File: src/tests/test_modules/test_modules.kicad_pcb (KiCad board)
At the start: 2 copper layers, 29.2 x 16.5 mm, 3 parts, among them U1 LM555, U2 LM555, U3 8255

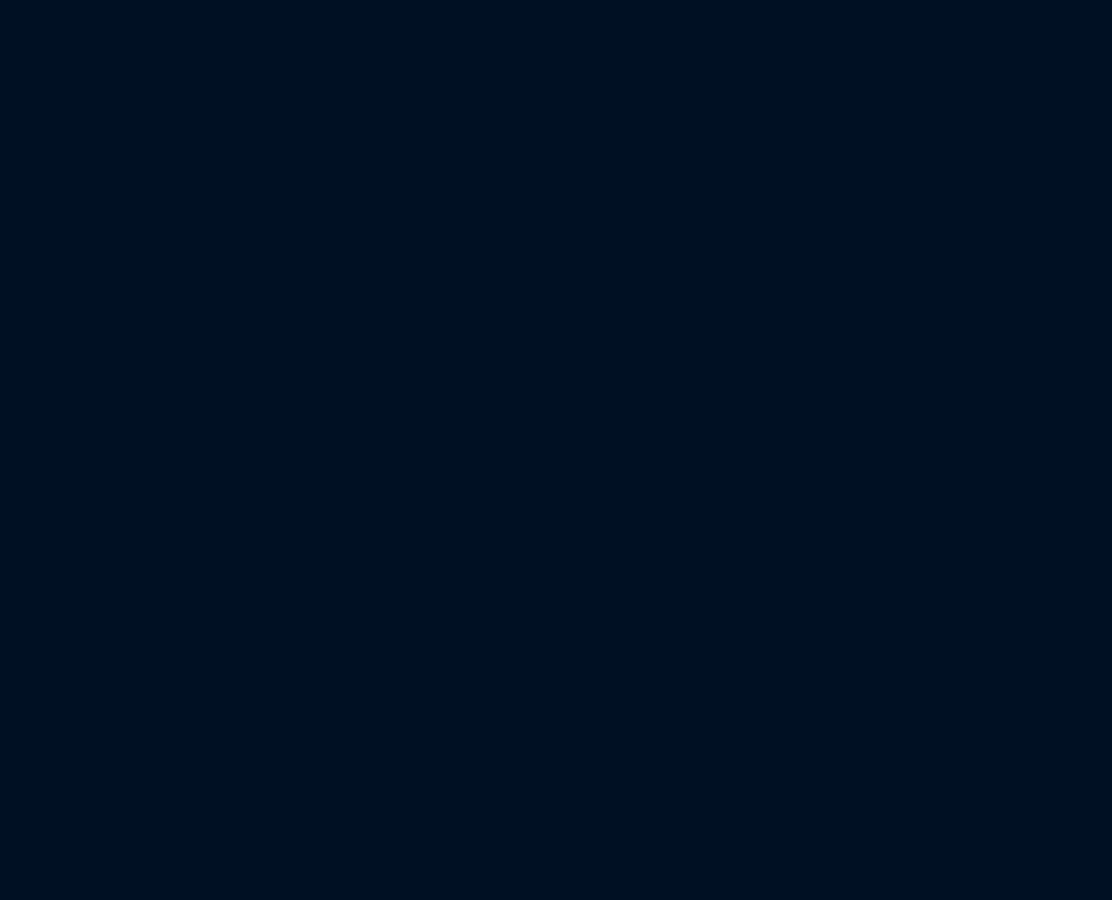
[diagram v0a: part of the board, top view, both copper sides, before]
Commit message: Add new keywords (#11)
Added new keywords:
`Modules Should Have Values Matching` - validate that selected modules have valid values.
`Complement Modules By Reference` - perform set complement operation on module lists.
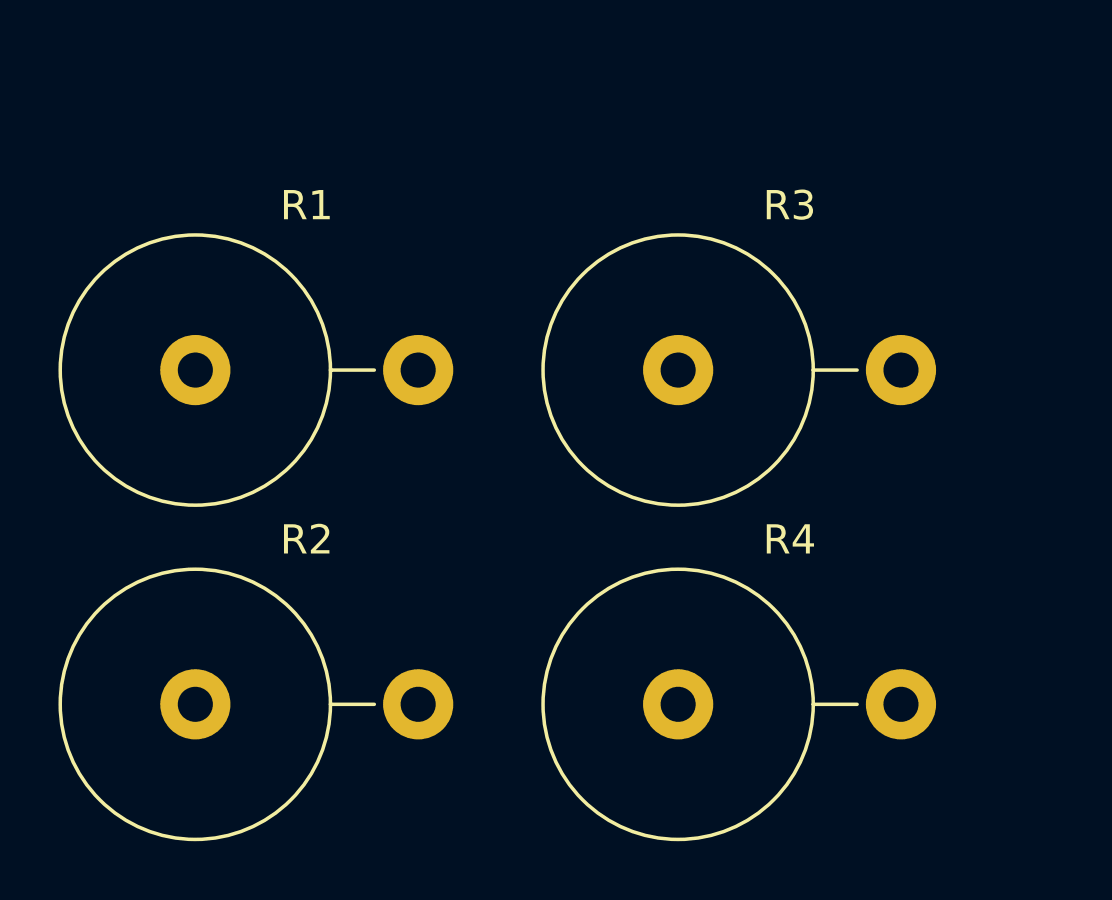
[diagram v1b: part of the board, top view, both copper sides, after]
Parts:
- added R1: 10k, Resistor_THT:R_Axial_DIN0922_L20.0mm_D9.0mm_P7.62mm_Vertical, F.Cu at (71.1, 74.9)
- added R2: 330, Resistor_THT:R_Axial_DIN0922_L20.0mm_D9.0mm_P7.62mm_Vertical, F.Cu at (71.1, 86.4)
- added R3: 2 M, Resistor_THT:R_Axial_DIN0922_L20.0mm_D9.0mm_P7.62mm_Vertical, F.Cu at (87.6, 74.9)
- added R4: 0.1uF, Resistor_THT:R_Axial_DIN0922_L20.0mm_D9.0mm_P7.62mm_Vertical, F.Cu at (87.6, 86.4)
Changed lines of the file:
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@@
     (tracks 39)
     (zones 0)
-    (modules 3)
-    (nets 49)
+    (modules 7)
+    (nets 57)
   )
   (page A4)
@@
   (net 47 "Net-(U3-Pad20)")
   (net 48 "Net-(U3-Pad40)")
+  (net 49 "Net-(R1-Pad1)")
+  (net 50 "Net-(R1-Pad2)")
+  (net 51 "Net-(R2-Pad2)")
+  (net 52 "Net-(R2-Pad1)")
+  (net 53 "Net-(R3-Pad1)")
+  (net 54 "Net-(R3-Pad2)")
+  (net 55 "Net-(R4-Pad2)")
+  (net 56 "Net-(R4-Pad1)")
   (net_class Default "This is the default net class."
     (clearance 0.2)
@@
     (add_net /~R)
     (add_net GND)
+    (add_net "Net-(R1-Pad1)")
+    (add_net "Net-(R1-Pad2)")
+    (add_net "Net-(R2-Pad1)")
+    (add_net "Net-(R2-Pad2)")
+    (add_net "Net-(R3-Pad1)")
+    (add_net "Net-(R3-Pad2)")
+    (add_net "Net-(R4-Pad1)")
+    (add_net "Net-(R4-Pad2)")
     (add_net "Net-(U3-Pad1)")
     (add_net "Net-(U3-Pad10)")
@@
     (add_net VCC)
   )
+  (module Resistor_THT:R_Axial_DIN0922_L20.0mm_D9.0mm_P7.62mm_Vertical (layer F.Cu)
+    (at 87.63 86.36)
+    (descr "Resistor, Axial_DIN0922 series, Axial, Vertical, pin pitch=7.62mm, 5W, length*diameter=20*9mm^2, http://www.vishay.com/docs/20128/wkxwrx.pdf")
+    (tags "Resistor Axial_DIN0922 series Axial Vertical pin pitch 7.62mm 5W length 20mm diameter 9mm")
+    (fp_text reference R4 (at 3.81 -5.62) (layer F.SilkS)
+      (effects (font (size 1 1) (thickness 0.15)))
+    )
+    (fp_text value 0.1uF (at 3.81 5.62) (layer F.Fab)
+      (effects (font (size 1 1) (thickness 0.15)))
+    )
+    (fp_text user %R (at 0 -1.7) (layer F.Fab)
+      (effects (font (size 1 1) (thickness 0.15)))
+    )
+    (fp_line (start 9.07 -4.75) (end -4.75 -4.75) (layer F.CrtYd) (width 0.05))
+    (fp_line (start 9.07 4.75) (end 9.07 -4.75) (layer F.CrtYd) (width 0.05))
+    (fp_line (start -4.75 4.75) (end 9.07 4.75) (layer F.CrtYd) (width 0.05))
+    (fp_line (start -4.75 -4.75) (end -4.75 4.75) (layer F.CrtYd) (width 0.05))
+    (fp_line (start 4.62 0) (end 6.12 0) (layer F.SilkS) (width 0.12))
+    (fp_line (start 0 0) (end 7.62 0) (layer F.Fab) (width 0.1))
+    (fp_circle (center 0 0) (end 4.62 0) (layer F.SilkS) (width 0.12))
+    (fp_circle (center 0 0) (end 4.5 0) (layer F.Fab) (width 0.1))
+    (pad 2 thru_hole oval (at 7.62 0) (size 2.4 2.4) (drill 1.2) (layers *.Cu *.Mask)
+      (net 55 "Net-(R4-Pad2)"))
+    (pad 1 thru_hole circle (at 0 0) (size 2.4 2.4) (drill 1.2) (layers *.Cu *.Mask)
+      (net 56 "Net-(R4-Pad1)"))
+    (model ${KISYS3DMOD}/Resistor_THT.3dshapes/R_Axial_DIN0922_L20.0mm_D9.0mm_P7.62mm_Vertical.wrl
+      (at (xyz 0 0 0))
+      (scale (xyz 1 1 1))
+      (rotate (xyz 0 0 0))
+    )
+  )
+  (module Resistor_THT:R_Axial_DIN0922_L20.0mm_D9.0mm_P7.62mm_Vertical (layer F.Cu)
+    (at 87.63 74.93)
+    (descr "Resistor, Axial_DIN0922 series, Axial, Vertical, pin pitch=7.62mm, 5W, length*diameter=20*9mm^2, http://www.vishay.com/docs/20128/wkxwrx.pdf")
+    (tags "Resistor Axial_DIN0922 series Axial Vertical pin pitch 7.62mm 5W length 20mm diameter 9mm")
+    (fp_text reference R3 (at 3.81 -5.62) (layer F.SilkS)
+      (effects (font (size 1 1) (thickness 0.15)))
+    )
+    (fp_text value "2 M" (at 3.81 5.62) (layer F.Fab)
+      (effects (font (size 1 1) (thickness 0.15)))
+    )
+    (fp_circle (center 0 0) (end 4.5 0) (layer F.Fab) (width 0.1))
+    (fp_circle (center 0 0) (end 4.62 0) (layer F.SilkS) (width 0.12))
+    (fp_line (start 0 0) (end 7.62 0) (layer F.Fab) (width 0.1))
+    (fp_line (start 4.62 0) (end 6.12 0) (layer F.SilkS) (width 0.12))
+    (fp_line (start -4.75 -4.75) (end -4.75 4.75) (layer F.CrtYd) (width 0.05))
+    (fp_line (start -4.75 4.75) (end 9.07 4.75) (layer F.CrtYd) (width 0.05))
+    (fp_line (start 9.07 4.75) (end 9.07 -4.75) (layer F.CrtYd) (width 0.05))
+    (fp_line (start 9.07 -4.75) (end -4.75 -4.75) (layer F.CrtYd) (width 0.05))
+    (fp_text user %R (at 0 -1.7) (layer F.Fab)
+      (effects (font (size 1 1) (thickness 0.15)))
+    )
+    (pad 1 thru_hole circle (at 0 0) (size 2.4 2.4) (drill 1.2) (layers *.Cu *.Mask)
+      (net 53 "Net-(R3-Pad1)"))
+    (pad 2 thru_hole oval (at 7.62 0) (size 2.4 2.4) (drill 1.2) (layers *.Cu *.Mask)
+      (net 54 "Net-(R3-Pad2)"))
+    (model ${KISYS3DMOD}/Resistor_THT.3dshapes/R_Axial_DIN0922_L20.0mm_D9.0mm_P7.62mm_Vertical.wrl
+      (at (xyz 0 0 0))
+      (scale (xyz 1 1 1))
+      (rotate (xyz 0 0 0))
+    )
+  )
+  (module Resistor_THT:R_Axial_DIN0922_L20.0mm_D9.0mm_P7.62mm_Vertical (layer F.Cu)
+    (at 71.12 86.36)
+    (descr "Resistor, Axial_DIN0922 series, Axial, Vertical, pin pitch=7.62mm, 5W, length*diameter=20*9mm^2, http://www.vishay.com/docs/20128/wkxwrx.pdf")
+    (tags "Resistor Axial_DIN0922 series Axial Vertical pin pitch 7.62mm 5W length 20mm diameter 9mm")
+    (fp_text reference R2 (at 3.81 -5.62) (layer F.SilkS)
+      (effects (font (size 1 1) (thickness 0.15)))
+    )
+    (fp_text value 330 (at 3.81 5.62) (layer F.Fab)
+      (effects (font (size 1 1) (thickness 0.15)))
+    )
+    (fp_text user %R (at 0 -1.7) (layer F.Fab)
+      (effects (font (size 1 1) (thickness 0.15)))
+    )
+    (fp_line (start 9.07 -4.75) (end -4.75 -4.75) (layer F.CrtYd) (width 0.05))
+    (fp_line (start 9.07 4.75) (end 9.07 -4.75) (layer F.CrtYd) (width 0.05))
+    (fp_line (start -4.75 4.75) (end 9.07 4.75) (layer F.CrtYd) (width 0.05))
+    (fp_line (start -4.75 -4.75) (end -4.75 4.75) (layer F.CrtYd) (width 0.05))
+    (fp_line (start 4.62 0) (end 6.12 0) (layer F.SilkS) (width 0.12))
+    (fp_line (start 0 0) (end 7.62 0) (layer F.Fab) (width 0.1))
+    (fp_circle (center 0 0) (end 4.62 0) (layer F.SilkS) (width 0.12))
+    (fp_circle (center 0 0) (end 4.5 0) (layer F.Fab) (width 0.1))
+    (pad 2 thru_hole oval (at 7.62 0) (size 2.4 2.4) (drill 1.2) (layers *.Cu *.Mask)
+      (net 51 "Net-(R2-Pad2)"))
+    (pad 1 thru_hole circle (at 0 0) (size 2.4 2.4) (drill 1.2) (layers *.Cu *.Mask)
+      (net 52 "Net-(R2-Pad1)"))
+    (model ${KISYS3DMOD}/Resistor_THT.3dshapes/R_Axial_DIN0922_L20.0mm_D9.0mm_P7.62mm_Vertical.wrl
+      (at (xyz 0 0 0))
+      (scale (xyz 1 1 1))
+      (rotate (xyz 0 0 0))
+    )
+  )
+  (module Resistor_THT:R_Axial_DIN0922_L20.0mm_D9.0mm_P7.62mm_Vertical (layer F.Cu)
+    (at 71.12 74.93)
+    (descr "Resistor, Axial_DIN0922 series, Axial, Vertical, pin pitch=7.62mm, 5W, length*diameter=20*9mm^2, http://www.vishay.com/docs/20128/wkxwrx.pdf")
+    (tags "Resistor Axial_DIN0922 series Axial Vertical pin pitch 7.62mm 5W length 20mm diameter 9mm")
+    (fp_text reference R1 (at 3.81 -5.62) (layer F.SilkS)
+      (effects (font (size 1 1) (thickness 0.15)))
+    )
+    (fp_text value 10k (at 3.81 5.62) (layer F.Fab)
+      (effects (font (size 1 1) (thickness 0.15)))
+    )
+    (fp_circle (center 0 0) (end 4.5 0) (layer F.Fab) (width 0.1))
+    (fp_circle (center 0 0) (end 4.62 0) (layer F.SilkS) (width 0.12))
+    (fp_line (start 0 0) (end 7.62 0) (layer F.Fab) (width 0.1))
+    (fp_line (start 4.62 0) (end 6.12 0) (layer F.SilkS) (width 0.12))
+    (fp_line (start -4.75 -4.75) (end -4.75 4.75) (layer F.CrtYd) (width 0.05))
+    (fp_line (start -4.75 4.75) (end 9.07 4.75) (layer F.CrtYd) (width 0.05))
+    (fp_line (start 9.07 4.75) (end 9.07 -4.75) (layer F.CrtYd) (width 0.05))
+    (fp_line (start 9.07 -4.75) (end -4.75 -4.75) (layer F.CrtYd) (width 0.05))
+    (fp_text user %R (at 0 -1.7) (layer F.Fab)
+      (effects (font (size 1 1) (thickness 0.15)))
+    )
+    (pad 1 thru_hole circle (at 0 0) (size 2.4 2.4) (drill 1.2) (layers *.Cu *.Mask)
+      (net 49 "Net-(R1-Pad1)"))
+    (pad 2 thru_hole oval (at 7.62 0) (size 2.4 2.4) (drill 1.2) (layers *.Cu *.Mask)
+      (net 50 "Net-(R1-Pad2)"))
+    (model ${KISYS3DMOD}/Resistor_THT.3dshapes/R_Axial_DIN0922_L20.0mm_D9.0mm_P7.62mm_Vertical.wrl
+      (at (xyz 0 0 0))
+      (scale (xyz 1 1 1))
+      (rotate (xyz 0 0 0))
+    )
+  )
   (module Package_DIP:DIP-40_W15.24mm (layer F.Cu)

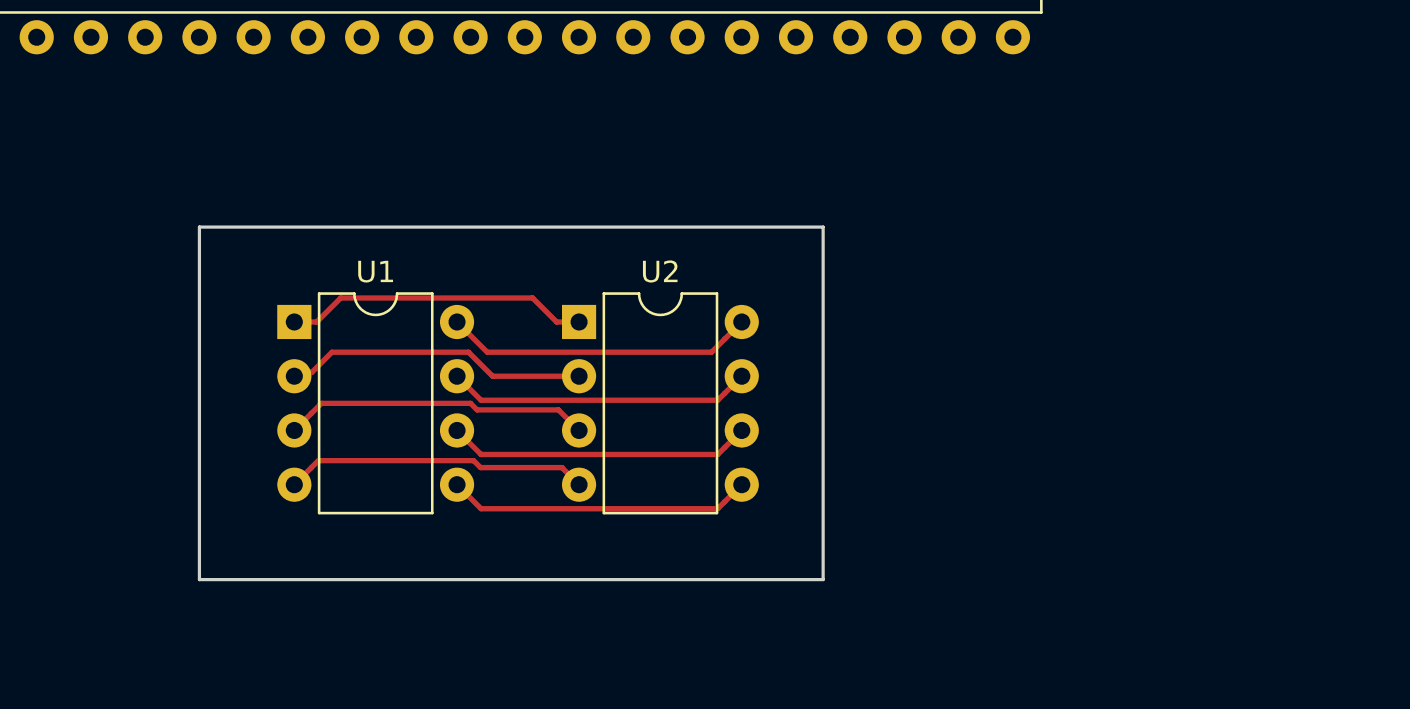
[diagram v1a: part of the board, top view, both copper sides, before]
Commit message: Adapt to newer versions of Robot Framework and KiCad, updating FOR loop syntax as well as deprecating LM555. Ensure Python3 is used. Stop building for Python 2.7 Fix code smell (is not -> !=). Update security token for GH releases.
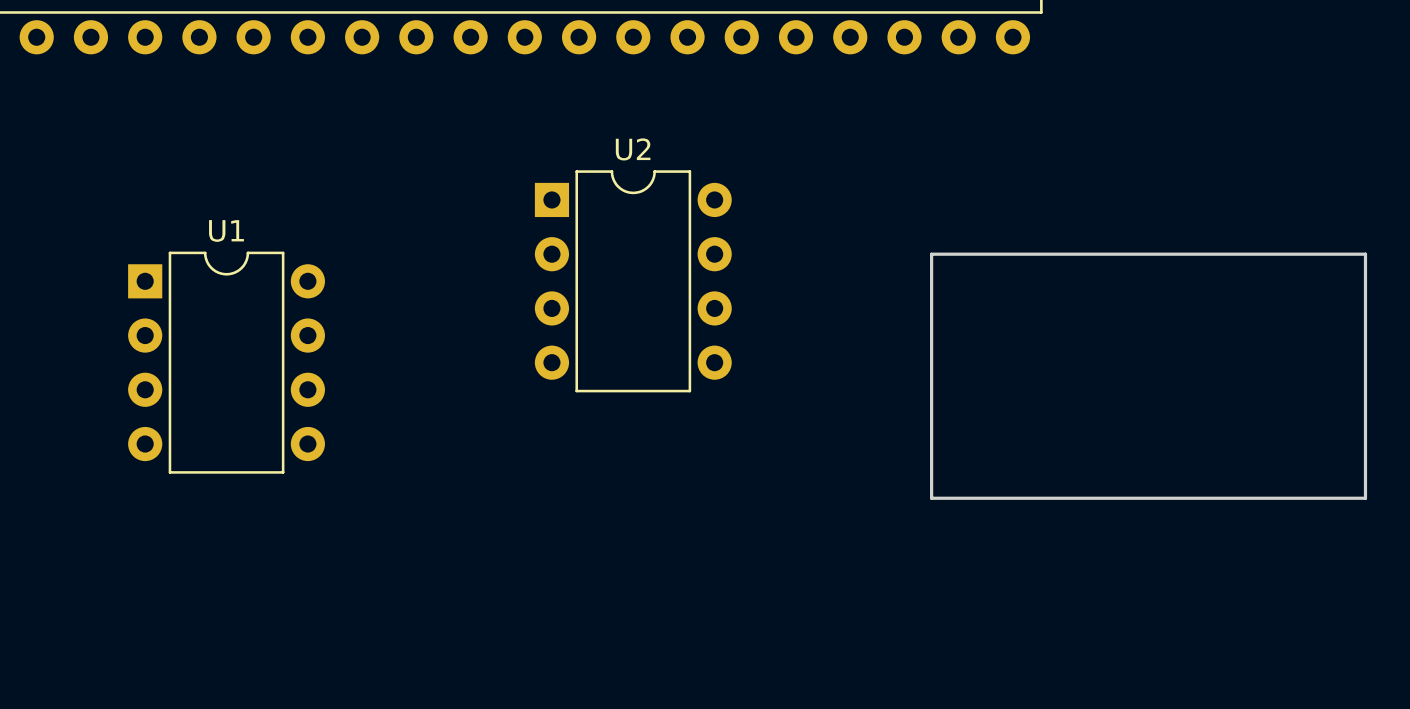
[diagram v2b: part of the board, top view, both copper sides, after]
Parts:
- U1, U2: value LM555 -> NA555P
- moved U1 7.24 mm to (116.8, 71.1)
- moved U2 5.85 mm to (135.9, 67.3)
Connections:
- R1 pad 1: Net-(R1-Pad1) -> (no net)
- R1 pad 2: Net-(R1-Pad2) -> (no net)
- R2 pad 1: Net-(R2-Pad1) -> (no net)
- R2 pad 2: Net-(R2-Pad2) -> (no net)
- R3 pad 1: Net-(R3-Pad1) -> (no net)
- R3 pad 2: Net-(R3-Pad2) -> (no net)
- R4 pad 1: Net-(R4-Pad1) -> (no net)
- R4 pad 2: Net-(R4-Pad2) -> (no net)
- U3 pad 1: Net-(U3-Pad1) -> (no net)
- U3 pad 10: Net-(U3-Pad10) -> (no net)
- U3 pad 11: Net-(U3-Pad11) -> (no net)
- U3 pad 12: Net-(U3-Pad12) -> (no net)
- U3 pad 13: Net-(U3-Pad13) -> (no net)
- U3 pad 14: Net-(U3-Pad14) -> (no net)
- U3 pad 15: Net-(U3-Pad15) -> (no net)
- U3 pad 16: Net-(U3-Pad16) -> (no net)
- U3 pad 17: Net-(U3-Pad17) -> (no net)
- U3 pad 18: Net-(U3-Pad18) -> (no net)
- U3 pad 19: Net-(U3-Pad19) -> (no net)
- U3 pad 2: Net-(U3-Pad2) -> (no net)
- U3 pad 20: Net-(U3-Pad20) -> (no net)
- U3 pad 21: Net-(U3-Pad21) -> (no net)
- U3 pad 22: Net-(U3-Pad22) -> (no net)
- U3 pad 23: Net-(U3-Pad23) -> (no net)
- U3 pad 24: Net-(U3-Pad24) -> (no net)
- U3 pad 25: Net-(U3-Pad25) -> (no net)
- U3 pad 26: Net-(U3-Pad26) -> (no net)
- U3 pad 27: Net-(U3-Pad27) -> (no net)
- U3 pad 28: Net-(U3-Pad28) -> (no net)
- U3 pad 29: Net-(U3-Pad29) -> (no net)
- U3 pad 3: Net-(U3-Pad3) -> (no net)
- U3 pad 30: Net-(U3-Pad30) -> (no net)
- U3 pad 31: Net-(U3-Pad31) -> (no net)
- U3 pad 32: Net-(U3-Pad32) -> (no net)
- U3 pad 33: Net-(U3-Pad33) -> (no net)
- U3 pad 34: Net-(U3-Pad34) -> (no net)
- U3 pad 35: Net-(U3-Pad35) -> (no net)
- U3 pad 36: Net-(U3-Pad36) -> (no net)
- U3 pad 37: Net-(U3-Pad37) -> (no net)
- U3 pad 38: Net-(U3-Pad38) -> (no net)
- U3 pad 39: Net-(U3-Pad39) -> (no net)
- U3 pad 4: Net-(U3-Pad4) -> (no net)
- U3 pad 40: Net-(U3-Pad40) -> (no net)
- U3 pad 5: Net-(U3-Pad5) -> (no net)
- U3 pad 6: Net-(U3-Pad6) -> (no net)
- U3 pad 7: Net-(U3-Pad7) -> (no net)
- U3 pad 8: Net-(U3-Pad8) -> (no net)
- U3 pad 9: Net-(U3-Pad9) -> (no net)
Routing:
- net VCC: track 14.5 -> 0.00 mm
- net /Q: track 14.4 -> 0.00 mm
- net /THR: track 14.3 -> 0.00 mm
- net /DIS: track 14.3 -> 0.00 mm
- net /CV: track 14.3 -> 0.00 mm
- net GND: track 14.3 -> 0.00 mm
- net /~R: track 14.3 -> 0.00 mm
- net /TR: track 13.9 -> 0.00 mm
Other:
- board size 29.2 x 16.5 mm -> 20.3 x 11.4 mm
